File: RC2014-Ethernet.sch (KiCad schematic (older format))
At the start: 24 parts

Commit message: Schematic, address layout, modified symbol
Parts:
- added TP?: IOCHRDY, symbol Connector:TestPoint_Alt
- added U?: RTL8019AS, symbol rtl8019as:RTL8019AS
- J1: renamed from J?; footprint (none) -> Connector_PinHeader_2.54mm:PinHeader_1x39_P2.54mm_Vertical
- J2: renamed from J?; footprint (none) -> Connector_Ethernet:8P8C_yellow_green_Ckmtw_C133529
- U1: renamed from U?; footprint (none) -> Package_QFP:PQFP-100_14x20mm_P0.65mm
- gave numbers to parts that had none: 20
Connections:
- net labels added: A0, A1, A2, A3, VCC, ~RD, ~RESET, ~WR
- wire segments 117 -> 150
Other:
- moved on the sheet: C1, C10, C2, C3, C4, C5, C6, C7, C8, C9, FB1, FB2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

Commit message: add address decoding and first traces
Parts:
- removed U?: RTL8019AS, symbol rtl8019as:RTL8019AS
- added C11: 100n, Capacitor_SMD:C_0402_1005Metric, symbol Device:C
- added FB?: Ferrite_Bead, Inductor_SMD:L_0805_2012Metric, symbol Device:Ferrite_Bead
- added J3: Address, Connector_PinHeader_2.54mm:PinHeader_2x08_P2.54mm_Vertical, symbol Connector_Generic:Conn_02x08_Odd_Even
- added R7: 200R, Resistor_SMD:R_0402_1005Metric, symbol Device:R
- added U2: 74LS138, Package_SO:SOIC-16_3.9x9.9mm_P1.27mm, symbol 74xx:74LS138
- TP1: renamed from TP?; footprint (none) -> TestPoint:TestPoint_Pad_2.5x2.5mm
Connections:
- net +5V: now also C11.1, U2.16 (VCC)
- net GND: now also C11.2, FB?.2, U2.4 (E1), U2.8 (GND); no longer C5.2, C6.1, J2.SH, U1.10 (A4)
- net ~AEN: now reaches U1.34 (*AEN)
- net ~AEN: now also J3.10 (Pin_10), J3.12 (Pin_12), J3.14 (Pin_14), J3.16 (Pin_16), J3.2 (Pin_2), J3.4 (Pin_4), J3.6 (Pin_6), J3.8 (Pin_8)
- net at U1.4 (INT0): now also R7.1
- net A6: now reaches J1.10 (A6)
- net A6: now also U2.2 (A1)
- net A5: now reaches J1.11 (A5)
- net A5: now also U2.1 (A0)
- net A4: now reaches J1.12 (A4)
- net A4: now also U1.10 (A4)
- net ~M1: now reaches J1.19 (~M1)
- net ~M1: now also U2.6 (E3)
- net ~INT: now reaches J1.22 (~INT)
- net ~INT: now also R7.2
- net ~IORQ: now reaches J1.26 (~IORQ)
- net ~IORQ: now also U2.5 (E2)
- net A7: now reaches J1.9 (A7)
- net A7: now also U2.3 (A2)
- new net: J3.11 (Pin_11), U2.10 (O5)
- new net: J3.9 (Pin_9), U2.11 (O4)
- new net: J3.7 (Pin_7), U2.12 (O3)
- new net: J3.5 (Pin_5), U2.13 (O2)
- new net: J3.3 (Pin_3), U2.14 (O1)
- new net: J3.1 (Pin_1), U2.15 (O0)
- new net: J3.15 (Pin_15), U2.7 (O7)
- new net: J3.13 (Pin_13), U2.9 (O6)
- new net Earth: C5.2, C6.1, FB?.1, J2.SH
- no-connect marks 28 -> 27

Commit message: Finish layout
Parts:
- removed FB1, FB2: Ferrite_Bead, Inductor_SMD:L_0805_2012Metric, symbol Device:Ferrite_Bead
- gave numbers to parts that had none: 1
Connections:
- net +5VA is gone; now on net +5V: C10.1, C9.1, U1.47 (AVCC), U1.57 (AVCC)
- net GNDA is gone; now on net GND: C10.2, C9.2, U1.44 (AGND), U1.52 (AGND)
- net VCC is gone; now on net +5V: U1.31 (SMEMRB), U1.32 (SMEMWB)
- net GND: now also Y1.2, Y1.4
- no-connect marks 27 -> 36
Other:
- moved on the sheet: C10, C9, FB3
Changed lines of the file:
@@
 Wire Wire Line
 	10450 6000 11000 6000
-Wire Wire Line
-	9350 6400 9450 6400
 $Comp
 L Device:C C7
@@
 L Device:C C9
 U 1 1 5F3421CA
-P 14650 4650
-F 0 "C9" H 14765 4696 50  0000 L CNN
-F 1 "100n" H 14765 4605 50  0000 L CNN
-F 2 "Capacitor_SMD:C_0402_1005Metric" H 14688 4500 50  0001 C CNN
-F 3 "~" H 14650 4650 50  0001 C CNN
-F 4 "C1525" H 14650 4650 50  0001 C CNN "LCSC"
-	1    14650 4650
+P 14050 4650
+F 0 "C9" H 14165 4696 50  0000 L CNN
+F 1 "100n" H 14165 4605 50  0000 L CNN
+F 2 "Capacitor_SMD:C_0402_1005Metric" H 14088 4500 50  0001 C CNN
+F 3 "~" H 14050 4650 50  0001 C CNN
+F 4 "C1525" H 14050 4650 50  0001 C CNN "LCSC"
+	1    14050 4650
 	1    0    0    -1
 $EndComp
@@
 L Device:C C10
 U 1 1 5F343CFF
-P 15100 4650
-F 0 "C10" H 15215 4696 50  0000 L CNN
-F 1 "100n" H 15215 4605 50  0000 L CNN
-F 2 "Capacitor_SMD:C_0402_1005Metric" H 15138 4500 50  0001 C CNN
-F 3 "~" H 15100 4650 50  0001 C CNN
-F 4 "C1525" H 15100 4650 50  0001 C CNN "LCSC"
-	1    15100 4650
+P 14250 4650
+F 0 "C10" H 14365 4696 50  0000 L CNN
+F 1 "100n" H 14365 4605 50  0000 L CNN
+F 2 "Capacitor_SMD:C_0402_1005Metric" H 14288 4500 50  0001 C CNN
+F 3 "~" H 14250 4650 50  0001 C CNN
+F 4 "C1525" H 14250 4650 50  0001 C CNN "LCSC"
+	1    14250 4650
 	1    0    0    -1
 $EndComp
@@
 Wire Wire Line
 	13650 4800 13650 5050
-$Comp
-L power:GNDA #PWR0105
-U 1 1 5F34C08E
-P 15400 4800
-F 0 "#PWR0105" H 15400 4550 50  0001 C CNN
-F 1 "GNDA" H 15405 4627 50  0000 C CNN
-F 2 "" H 15400 4800 50  0001 C CNN
-F 3 "" H 15400 4800 50  0001 C CNN
-	1    15400 4800
-	1    0    0    -1
-$EndComp
-$Comp
-L power:+5VA #PWR0106
-U 1 1 5F34CC61
-P 15400 4500
-F 0 "#PWR0106" H 15400 4350 50  0001 C CNN
-F 1 "+5VA" H 15415 4673 50  0000 C CNN
-F 2 "" H 15400 4500 50  0001 C CNN
-F 3 "" H 15400 4500 50  0001 C CNN
-	1    15400 4500
-	1    0    0    -1
-$EndComp
-Wire Wire Line
-	15400 4500 15100 4500
-Connection ~ 15100 4500
-Wire Wire Line
-	15100 4500 14650 4500
-Wire Wire Line
-	14650 4800 15100 4800
-Connection ~ 15100 4800
-Wire Wire Line
-	15100 4800 15400 4800
-$Comp
-L Device:Ferrite_Bead FB1
-U 1 1 5F35165F
-P 14200 4500
-F 0 "FB1" V 13926 4500 50  0000 C CNN
-F 1 "Ferrite_Bead" V 14017 4500 50  0000 C CNN
-F 2 "Inductor_SMD:L_0805_2012Metric" V 14130 4500 50  0001 C CNN
-F 3 "~" H 14200 4500 50  0001 C CNN
-F 4 "C1017" V 14200 4500 50  0001 C CNN "LCSC"
-	1    14200 4500
-	0    1    1    0
-$EndComp
-$Comp
-L Device:Ferrite_Bead FB2
-U 1 1 5F3536E2
-P 14200 4800
-F 0 "FB2" V 13926 4800 50  0000 C CNN
-F 1 "Ferrite_Bead" V 14017 4800 50  0000 C CNN
-F 2 "Inductor_SMD:L_0805_2012Metric" V 14130 4800 50  0001 C CNN
-F 3 "~" H 14200 4800 50  0001 C CNN
-F 4 "C1017" V 14200 4800 50  0001 C CNN "LCSC"
-	1    14200 4800
-	0    -1   -1   0
-$EndComp
+Wire Wire Line
+	14050 4800 14250 4800
 Wire Wire Line
 	14050 4800 13850 4800
 Wire Wire Line
 	13650 4500 13850 4500
-Wire Wire Line
-	14350 4500 14650 4500
-Connection ~ 14650 4500
-Wire Wire Line
-	14650 4800 14350 4800
-Connection ~ 14650 4800
-$Comp
-L power:GNDA #PWR0107
-U 1 1 5F35E6C9
-P 9450 6400
-F 0 "#PWR0107" H 9450 6150 50  0001 C CNN
-F 1 "GNDA" H 9455 6227 50  0000 C CNN
-F 2 "" H 9450 6400 50  0001 C CNN
-F 3 "" H 9450 6400 50  0001 C CNN
-	1    9450 6400
-	1    0    0    -1
-$EndComp
-$Comp
-L power:+5VA #PWR0108
-U 1 1 5F35E6CF
-P 9450 850
-F 0 "#PWR0108" H 9450 700 50  0001 C CNN
-F 1 "+5VA" H 9465 1023 50  0000 C CNN
-F 2 "" H 9450 850 50  0001 C CNN
-F 3 "" H 9450 850 50  0001 C CNN
-	1    9450 850
-	1    0    0    -1
-$EndComp
-Connection ~ 9450 6400
-Wire Wire Line
-	9450 900  9450 850
-Wire Wire Line
-	9450 900  9350 900
-Connection ~ 9450 900
 NoConn ~ 10350 4500
 NoConn ~ 10350 4600
@@
 Wire Wire Line
 	13850 4800 13650 4800
-$Comp
-L power:GND #PWR0111
-U 1 1 5F340133
-P 12950 5050
-F 0 "#PWR0111" H 12950 4800 50  0001 C CNN
-F 1 "GND" H 12955 4877 50  0000 C CNN
-F 2 "" H 12950 5050 50  0001 C CNN
-F 3 "" H 12950 5050 50  0001 C CNN
-	1    12950 5050
-	1    0    0    -1
-$EndComp
 NoConn ~ 10350 3700
 NoConn ~ 10350 3800
@@
 	13250 5050 13350 5050
 Connection ~ 13350 5050
-Connection ~ 12950 5050
 Wire Wire Line
 	13350 4250 13450 4250
@@
 	8350 5100 8350 5000
 Connection ~ 8550 5100
-$Comp
-L power:VCC #PWR0119
-U 1 1 5F36D474
-P 8350 5000
-F 0 "#PWR0119" H 8350 4850 50  0001 C CNN
-F 1 "VCC" H 8365 5173 50  0000 C CNN
-F 2 "" H 8350 5000 50  0001 C CNN
-F 3 "" H 8350 5000 50  0001 C CNN
-	1    8350 5000
-	1    0    0    -1
-$EndComp
 Text Label 8350 5600 0    50   ~ 0
 ~WR
@@
 Wire Wire Line
 	10850 4400 10650 4400
-$Comp
-L Device:Ferrite_Bead FB?
-U 1 1 5F59AA0A
-P 14750 5650
-F 0 "FB?" V 14476 5650 50  0000 C CNN
-F 1 "Ferrite_Bead" V 14567 5650 50  0000 C CNN
-F 2 "Inductor_SMD:L_0805_2012Metric" V 14680 5650 50  0001 C CNN
-F 3 "~" H 14750 5650 50  0001 C CNN
-F 4 "C1017" V 14750 5650 50  0001 C CNN "LCSC"
-	1    14750 5650
-	0    1    1    0
-$EndComp
-$Comp
-L power:GND #PWR?
-U 1 1 5F5D0203
-P 14450 5650
-F 0 "#PWR?" H 14450 5400 50  0001 C CNN
-F 1 "GND" H 14455 5477 50  0000 C CNN
-F 2 "" H 14450 5650 50  0001 C CNN
-F 3 "" H 14450 5650 50  0001 C CNN
-	1    14450 5650
-	1    0    0    -1
-$EndComp
-$Comp
-L power:Earth #PWR?
-U 1 1 5F5D100D
-P 15050 5650
-F 0 "#PWR?" H 15050 5400 50  0001 C CNN
-F 1 "Earth" H 15050 5500 50  0001 C CNN
-F 2 "" H 15050 5650 50  0001 C CNN
-F 3 "~" H 15050 5650 50  0001 C CNN
-	1    15050 5650
-	1    0    0    -1
-$EndComp
-Wire Wire Line
-	15050 5650 14900 5650
-Wire Wire Line
-	14450 5650 14600 5650
 Wire Wire Line
 	13050 3050 13150 3050
 $Comp
-L power:Earth #PWR?
+L power:Earth #PWR0124
 U 1 1 5F6147A0
 P 13150 3050
-F 0 "#PWR?" H 13150 2800 50  0001 C CNN
+F 0 "#PWR0124" H 13150 2800 50  0001 C CNN
 F 1 "Earth" H 13150 2900 50  0001 C CNN
 F 2 "" H 13150 3050 50  0001 C CNN
@@
 	13150 3050 13250 3050
 $Comp
-L power:Earth #PWR?
+L power:Earth #PWR0125
 U 1 1 5F614F60
 P 14100 1200
-F 0 "#PWR?" H 14100 950 50  0001 C CNN
+F 0 "#PWR0125" H 14100 950 50  0001 C CNN
 F 1 "Earth" H 14100 1050 50  0001 C CNN
 F 2 "" H 14100 1200 50  0001 C CNN
@@
 	1    0    0    -1
 $EndComp
+$Comp
+L power:+5V #PWR0119
+U 1 1 5F661D52
+P 8350 5000
+F 0 "#PWR0119" H 8350 4850 50  0001 C CNN
+F 1 "+5V" H 8365 5173 50  0000 C CNN
+F 2 "" H 8350 5000 50  0001 C CNN
+F 3 "" H 8350 5000 50  0001 C CNN
+	1    8350 5000
+	1    0    0    -1
+$EndComp
+Connection ~ 14050 4500
+Connection ~ 14050 4800
+Wire Wire Line
+	14250 4500 14050 4500
+Connection ~ 12950 5050
+Wire Wire Line
+	13150 5550 13300 5550
+Wire Wire Line
+	13750 5550 13600 5550
+$Comp
+L power:Earth #PWR0110
+U 1 1 5F5D100D
+P 13750 5550
+F 0 "#PWR0110" H 13750 5300 50  0001 C CNN
+F 1 "Earth" H 13750 5400 50  0001 C CNN
+F 2 "" H 13750 5550 50  0001 C CNN
+F 3 "~" H 13750 5550 50  0001 C CNN
+	1    13750 5550
+	1    0    0    -1
+$EndComp
+$Comp
+L power:GND #PWR0101
+U 1 1 5F5D0203
+P 13150 5550
+F 0 "#PWR0101" H 13150 5300 50  0001 C CNN
+F 1 "GND" H 13155 5377 50  0000 C CNN
+F 2 "" H 13150 5550 50  0001 C CNN
+F 3 "" H 13150 5550 50  0001 C CNN
+	1    13150 5550
+	1    0    0    -1
+$EndComp
+$Comp
+L Device:Ferrite_Bead FB3
+U 1 1 5F59AA0A
+P 13450 5550
+F 0 "FB3" V 13176 5550 50  0000 C CNN
+F 1 "Ferrite_Bead" V 13267 5550 50  0000 C CNN
+F 2 "Inductor_SMD:L_0805_2012Metric" V 13380 5550 50  0001 C CNN
+F 3 "~" H 13450 5550 50  0001 C CNN
+F 4 "C1017" V 13450 5550 50  0001 C CNN "LCSC"
+	1    13450 5550
+	0    1    1    0
+$EndComp
+$Comp
+L power:GND #PWR0111
+U 1 1 5F340133
+P 12950 5050
+F 0 "#PWR0111" H 12950 4800 50  0001 C CNN
+F 1 "GND" H 12955 4877 50  0000 C CNN
+F 2 "" H 12950 5050 50  0001 C CNN
+F 3 "" H 12950 5050 50  0001 C CNN
+	1    12950 5050
+	1    0    0    -1
+$EndComp
+$Comp
+L power:GND #PWR0105
+U 1 1 5F6F7F19
+P 9350 6400
+F 0 "#PWR0105" H 9350 6150 50  0001 C CNN
+F 1 "GND" H 9355 6227 50  0000 C CNN
+F 2 "" H 9350 6400 50  0001 C CNN
+F 3 "" H 9350 6400 50  0001 C CNN
+	1    9350 6400
+	1    0    0    -1
+$EndComp
+Wire Wire Line
+	9350 6400 9450 6400
+Connection ~ 9350 6400
+Wire Wire Line
+	9350 900  9450 900
+$Comp
+L power:+5V #PWR0106
+U 1 1 5F71CF68
+P 9350 900
+F 0 "#PWR0106" H 9350 750 50  0001 C CNN
+F 1 "+5V" H 9365 1073 50  0000 C CNN
+F 2 "" H 9350 900 50  0001 C CNN
+F 3 "" H 9350 900 50  0001 C CNN
+	1    9350 900
+	1    0    0    -1
+$EndComp
+Connection ~ 9350 900
+NoConn ~ 1700 1200
+NoConn ~ 1700 1300
+NoConn ~ 1700 1400
+NoConn ~ 1700 1500
+NoConn ~ 1700 1600
+NoConn ~ 1700 1700
+NoConn ~ 1700 1800
+NoConn ~ 1700 1900
+NoConn ~ 1700 3200
+Wire Wire Line
+	10800 5750 10800 6200
+Wire Wire Line
+	11200 5750 11200 6200
+Wire Wire Line
+	11200 6200 11000 6200
+$Comp
+L power:GND #PWR0107
+U 1 1 5F7A2065
+P 11000 6200
+F 0 "#PWR0107" H 11000 5950 50  0001 C CNN
+F 1 "GND" H 11005 6027 50  0000 C CNN
+F 2 "" H 11000 6200 50  0001 C CNN
+F 3 "" H 11000 6200 50  0001 C CNN
+	1    11000 6200
+	1    0    0    -1
+$EndComp
+Connection ~ 11000 6200
+Wire Wire Line
+	11000 6200 10800 6200
 $EndSCHEMATC

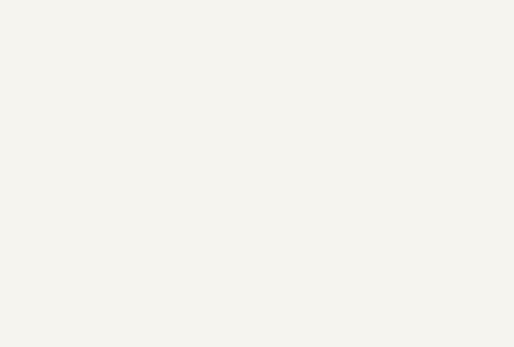
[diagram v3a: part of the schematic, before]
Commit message: RevA, Tooling holes, via stitching
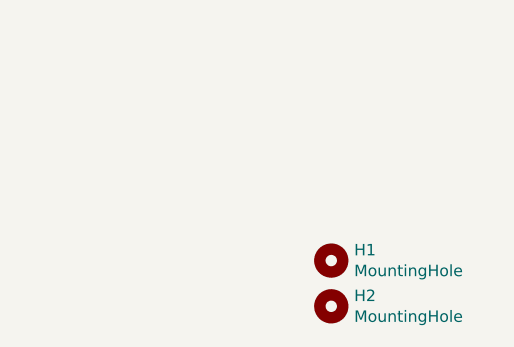
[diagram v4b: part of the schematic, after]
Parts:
- added H1, H2: MountingHole, ToolingHole:ToolingHole_JLCSMT, symbol Mechanical:MountingHole
- C1, C2, C5, C6: LCSC C20037 -> C9196
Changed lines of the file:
@@
 F 2 "Capacitor_SMD:C_1206_3216Metric" H 11438 2750 50  0001 C CNN
 F 3 "~" H 11400 2900 50  0001 C CNN
-F 4 "C20037" H 11400 2900 50  0001 C CNN "LCSC"
+F 4 "C9196" H 11400 2900 50  0001 C CNN "LCSC"
 	1    11400 2900
 	1    0    0    -1
@@
 F 2 "Capacitor_SMD:C_1206_3216Metric" H 11238 2750 50  0001 C CNN
 F 3 "~" H 11200 2900 50  0001 C CNN
-F 4 "C20037" H 11200 2900 50  0001 C CNN "LCSC"
+F 4 "C9196" H 11200 2900 50  0001 C CNN "LCSC"
 	1    11200 2900
 	-1   0    0    1
@@
 F 2 "Capacitor_SMD:C_1206_3216Metric" H 13088 2750 50  0001 C CNN
 F 3 "~" H 13050 2900 50  0001 C CNN
-F 4 "C20037" H 13050 2900 50  0001 C CNN "LCSC"
+F 4 "C9196" H 13050 2900 50  0001 C CNN "LCSC"
 	1    13050 2900
 	-1   0    0    -1
-$EndComp
-$Comp
-L Device:C C6
-U 1 1 5F3B4B89
-P 13250 2900
-F 0 "C6" H 13365 2946 50  0000 L CNN
-F 1 "1nF" H 13365 2855 50  0000 L CNN
-F 2 "Capacitor_SMD:C_1206_3216Metric" H 13288 2750 50  0001 C CNN
-F 3 "~" H 13250 2900 50  0001 C CNN
-F 4 "C20037" H 13250 2900 50  0001 C CNN "LCSC"
-	1    13250 2900
-	1    0    0    1
 $EndComp
 Wire Wire Line
@@
 Wire Wire Line
 	11000 6200 10800 6200
+$Comp
+L Mechanical:MountingHole H2
+U 1 1 5F81BBE4
+P 15300 9500
+F 0 "H2" H 15400 9546 50  0000 L CNN
+F 1 "MountingHole" H 15400 9455 50  0000 L CNN
+F 2 "ToolingHole:ToolingHole_JLCSMT" H 15300 9500 50  0001 C CNN
+F 3 "~" H 15300 9500 50  0001 C CNN
+	1    15300 9500
+	1    0    0    -1
+$EndComp
+$Comp
+L Mechanical:MountingHole H1
+U 1 1 5F8298D3
+P 15300 9300
+F 0 "H1" H 15400 9346 50  0000 L CNN
+F 1 "MountingHole" H 15400 9255 50  0000 L CNN
+F 2 "ToolingHole:ToolingHole_JLCSMT" H 15300 9300 50  0001 C CNN
+F 3 "~" H 15300 9300 50  0001 C CNN
+	1    15300 9300
+	1    0    0    -1
+$EndComp
+$Comp
+L Device:C C6
+U 1 1 5F3B4B89
+P 13250 2900
+F 0 "C6" H 13365 2946 50  0000 L CNN
+F 1 "1nF" H 13365 2855 50  0000 L CNN
+F 2 "Capacitor_SMD:C_1206_3216Metric" H 13288 2750 50  0001 C CNN
+F 3 "~" H 13250 2900 50  0001 C CNN
+F 4 "C9196" H 13250 2900 50  0001 C CNN "LCSC"
+	1    13250 2900
+	1    0    0    1
+$EndComp
 $EndSCHEMATC
